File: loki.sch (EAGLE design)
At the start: 53 parts, among them IC2 LM358D, Q1 MOSFET-PCHANNELSMD, U1 USD SOCKET, X1 USBSMD, Y1 XRCGB_XTAL

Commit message: Minor layout changes; improvements to 2 pin plank template.
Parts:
- R3: device resistor:R-US_R0805 -> resistor:R-US_R0603
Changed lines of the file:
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@@
 <part name="GND18" library="supply1" deviceset="GND" device=""/>
 <part name="LED1" library="led" deviceset="LED" device="CHIP-LED0805"/>
-<part name="R3" library="resistor" deviceset="R-US_" device="R0805" value="330"/>
+<part name="R3" library="resistor" deviceset="R-US_" device="R0603" value="330"/>
 <part name="GND19" library="supply1" deviceset="GND" device=""/>
 <part name="SV1" library="con-lsta" deviceset="FE10-1" device=""/>

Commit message: Added reverse polarity protection diode.
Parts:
- added D3: (no value), adafruit:DIODESMA
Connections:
- new net N$11: CN1.PWR, D3.A
- net V+: now also D3.C; no longer CN1.PWR
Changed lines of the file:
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@@
 <part name="VCC1" library="supply1" deviceset="+3V3" device=""/>
 <part name="FRAME1" library="SparkFun-Aesthetics" deviceset="FRAME-A3" device=""/>
+<part name="D3" library="adafruit" deviceset="DIODE" device="SMA"/>
 </parts>
 <sheets>
@@
 <instance part="VCC1" gate="G$1" x="457.2" y="198.12"/>
 <instance part="FRAME1" gate="G$1" x="279.4" y="-45.72"/>
+<instance part="D3" gate="G$1" x="556.26" y="182.88"/>
 </instances>
 <busses>
@@
 <junction x="563.88" y="182.88"/>
 <junction x="561.34" y="182.88"/>
-<pinref part="CN1" gate="G$1" pin="PWR"/>
-<wire x1="561.34" y1="182.88" x2="551.18" y2="182.88" width="0.1524" layer="91"/>
+<pinref part="D3" gate="G$1" pin="C"/>
+<wire x1="558.8" y1="182.88" x2="561.34" y2="182.88" width="0.1524" layer="91"/>
 </segment>
 <segment>
@@
 </segment>
 </net>
+<net name="N$11" class="0">
+<segment>
+<pinref part="CN1" gate="G$1" pin="PWR"/>
+<pinref part="D3" gate="G$1" pin="A"/>
+<wire x1="551.18" y1="182.88" x2="553.72" y2="182.88" width="0.1524" layer="91"/>
+</segment>
+</net>

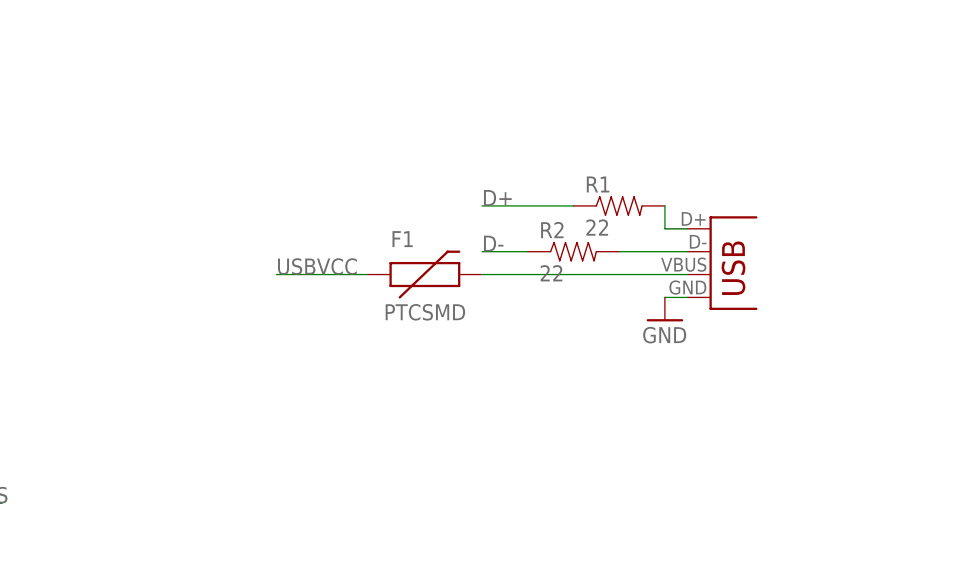
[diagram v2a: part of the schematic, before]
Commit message: Replace usb mini connector with usb micro one.
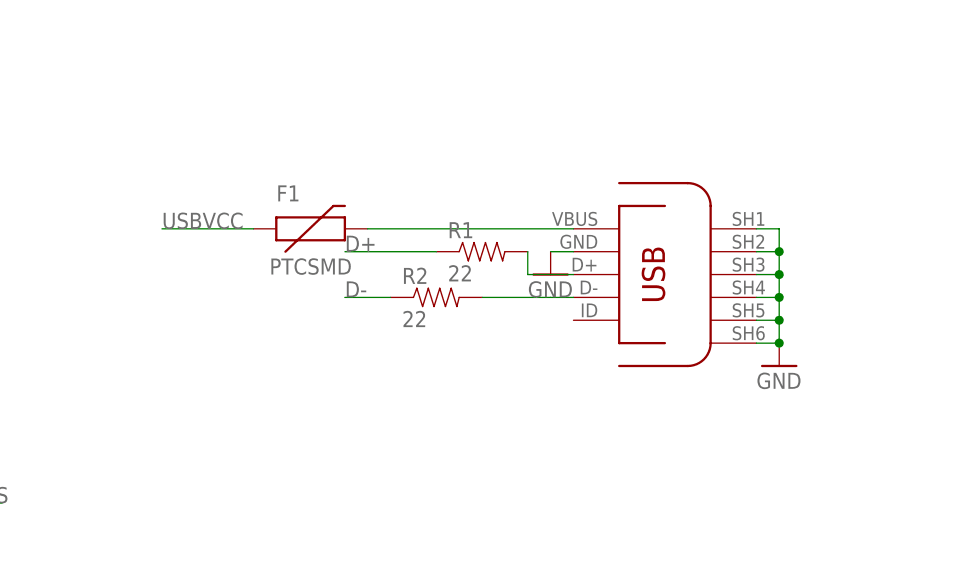
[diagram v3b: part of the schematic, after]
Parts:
- removed X1: USBSMD, SparkFun-Connectors:USBSMD
- added U$7: MICROUSB, ondraster:MICROUSB
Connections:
- net GND: now also U$7.GND, U$7.SH@1, U$7.SH@2, U$7.SH@3, U$7.SH@4, U$7.SH@5, U$7.SH@6; no longer X1.GND
- net N$15: now also U$7.VCC; no longer X1.VBUS
- net N$2: now also U$7.D-; no longer X1.D-
- net N$4: now also U$7.D+; no longer X1.D+
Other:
- moved on the sheet: F1, R1, R2
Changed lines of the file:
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@@
 <part name="R1" library="SparkFun-Passives" deviceset="RESISTOR" device="0603-RES" value="22"/>
 <part name="R2" library="SparkFun-Passives" deviceset="RESISTOR" device="0603-RES" value="22"/>
-<part name="X1" library="SparkFun-Connectors" deviceset="USB" device="SMD"/>
 <part name="P+1" library="supply1" deviceset="+3V3" device=""/>
 <part name="C3" library="resistor" deviceset="C-EU" device="C0603K" value="0.1u"/>
@@
 <part name="FRAME1" library="SparkFun-Aesthetics" deviceset="FRAME-A3" device=""/>
 <part name="D3" library="adafruit" deviceset="DIODE" device="SMA"/>
+<part name="U$7" library="ondraster" deviceset="MICROUSB" device=""/>
+<part name="GND2" library="supply1" deviceset="GND" device=""/>
 </parts>
 <sheets>
@@
 </plain>
 <instances>
-<instance part="R1" gate="G$1" x="482.6" y="101.6"/>
-<instance part="R2" gate="G$1" x="477.52" y="96.52"/>
-<instance part="X1" gate="G$1" x="492.76" y="91.44"/>
+<instance part="R1" gate="G$1" x="467.36" y="96.52"/>
+<instance part="R2" gate="G$1" x="462.28" y="91.44"/>
 <instance part="P+1" gate="G$1" x="309.88" y="71.12" rot="R90"/>
 <instance part="C3" gate="G$1" x="332.74" y="66.04"/>
@@
 <instance part="GND8" gate="1" x="464.82" y="180.34"/>
 <instance part="C17" gate="G$1" x="457.2" y="190.5"/>
-<instance part="GND9" gate="1" x="487.68" y="88.9"/>
+<instance part="GND9" gate="1" x="474.98" y="93.98"/>
 <instance part="U$3" gate="G$1" x="579.12" y="172.72"/>
 <instance part="P+5" gate="1" x="561.34" y="187.96"/>
@@
 <instance part="GND13" gate="1" x="614.68" y="22.86"/>
 <instance part="P+10" gate="1" x="647.7" y="58.42"/>
-<instance part="F1" gate="G$1" x="459.74" y="93.98"/>
+<instance part="F1" gate="G$1" x="447.04" y="99.06"/>
 <instance part="CN1" gate="G$1" x="548.64" y="180.34"/>
 <instance part="Y1" gate="G$1" x="388.62" y="104.14" rot="R90"/>
@@
 <instance part="FRAME1" gate="G$1" x="279.4" y="-45.72"/>
 <instance part="D3" gate="G$1" x="556.26" y="182.88"/>
+<instance part="U$7" gate="G$1" x="482.6" y="93.98" rot="MR0"/>
+<instance part="GND2" gate="1" x="500.38" y="83.82"/>
 </instances>
 <busses>
@@
 </segment>
 <segment>
-<pinref part="X1" gate="G$1" pin="GND"/>
 <pinref part="GND9" gate="1" pin="GND"/>
-<wire x1="490.22" y1="91.44" x2="487.68" y2="91.44" width="0.1524" layer="91"/>
+<wire x1="477.52" y1="96.52" x2="474.98" y2="96.52" width="0.1524" layer="91"/>
+<pinref part="U$7" gate="G$1" pin="GND"/>
 </segment>
 <segment>
@@
 <junction x="383.54" y="7.62"/>
 </segment>
+<segment>
+<pinref part="U$7" gate="G$1" pin="SH@1"/>
+<pinref part="GND2" gate="1" pin="GND"/>
+<wire x1="497.84" y1="99.06" x2="500.38" y2="99.06" width="0.1524" layer="91"/>
+<wire x1="500.38" y1="99.06" x2="500.38" y2="96.52" width="0.1524" layer="91"/>
+<pinref part="U$7" gate="G$1" pin="SH@6"/>
+<wire x1="500.38" y1="96.52" x2="500.38" y2="93.98" width="0.1524" layer="91"/>
+<wire x1="500.38" y1="93.98" x2="500.38" y2="91.44" width="0.1524" layer="91"/>
+<wire x1="500.38" y1="91.44" x2="500.38" y2="88.9" width="0.1524" layer="91"/>
+<wire x1="500.38" y1="88.9" x2="500.38" y2="86.36" width="0.1524" layer="91"/>
+<wire x1="500.38" y1="86.36" x2="497.84" y2="86.36" width="0.1524" layer="91"/>
+<junction x="500.38" y="86.36"/>
+<pinref part="U$7" gate="G$1" pin="SH@5"/>
+<wire x1="500.38" y1="88.9" x2="497.84" y2="88.9" width="0.1524" layer="91"/>
+<junction x="500.38" y="88.9"/>
+<pinref part="U$7" gate="G$1" pin="SH@4"/>
+<wire x1="500.38" y1="91.44" x2="497.84" y2="91.44" width="0.1524" layer="91"/>
+<junction x="500.38" y="91.44"/>
+<pinref part="U$7" gate="G$1" pin="SH@3"/>
+<wire x1="500.38" y1="93.98" x2="497.84" y2="93.98" width="0.1524" layer="91"/>
+<junction x="500.38" y="93.98"/>
+<pinref part="U$7" gate="G$1" pin="SH@2"/>
+<wire x1="500.38" y1="96.52" x2="497.84" y2="96.52" width="0.1524" layer="91"/>
+<junction x="500.38" y="96.52"/>
+</segment>
 </net>
 <net name="+5V" class="0">
@@
 <net name="N$2" class="0">
 <segment>
-<pinref part="X1" gate="G$1" pin="D-"/>
 <pinref part="R2" gate="G$1" pin="2"/>
-<wire x1="490.22" y1="96.52" x2="482.6" y2="96.52" width="0.1524" layer="91"/>
+<wire x1="474.98" y1="91.44" x2="467.36" y2="91.44" width="0.1524" layer="91"/>
+<pinref part="U$7" gate="G$1" pin="D-"/>
+<wire x1="477.52" y1="91.44" x2="474.98" y2="91.44" width="0.1524" layer="91"/>
 </segment>
 </net>
@@
 <segment>
 <pinref part="R1" gate="G$1" pin="2"/>
-<wire x1="487.68" y1="101.6" x2="487.68" y2="99.06" width="0.1524" layer="91"/>
-<pinref part="X1" gate="G$1" pin="D+"/>
-<wire x1="487.68" y1="99.06" x2="490.22" y2="99.06" width="0.1524" layer="91"/>
+<wire x1="472.44" y1="96.52" x2="472.44" y2="93.98" width="0.1524" layer="91"/>
+<wire x1="472.44" y1="93.98" x2="474.98" y2="93.98" width="0.1524" layer="91"/>
+<pinref part="U$7" gate="G$1" pin="D+"/>
+<wire x1="474.98" y1="93.98" x2="477.52" y2="93.98" width="0.1524" layer="91"/>
 </segment>
 </net>
@@
 <segment>
 <pinref part="R1" gate="G$1" pin="1"/>
-<wire x1="477.52" y1="101.6" x2="467.36" y2="101.6" width="0.1524" layer="91"/>
-<label x="467.36" y="101.6" size="1.778" layer="95"/>
+<wire x1="462.28" y1="96.52" x2="452.12" y2="96.52" width="0.1524" layer="91"/>
+<label x="452.12" y="96.52" size="1.778" layer="95"/>
 </segment>
 <segment>
@@
 <segment>
 <pinref part="R2" gate="G$1" pin="1"/>
-<wire x1="467.36" y1="96.52" x2="472.44" y2="96.52" width="0.1524" layer="91"/>
-<label x="467.36" y="96.52" size="1.778" layer="95"/>
+<wire x1="452.12" y1="91.44" x2="457.2" y2="91.44" width="0.1524" layer="91"/>
+<label x="452.12" y="91.44" size="1.778" layer="95"/>
 </segment>
 <segment>
@@
 <segment>
 <pinref part="F1" gate="G$1" pin="1"/>
-<wire x1="454.66" y1="93.98" x2="444.5" y2="93.98" width="0.1524" layer="91"/>
-<label x="444.5" y="93.98" size="1.778" layer="95"/>
+<wire x1="441.96" y1="99.06" x2="431.8" y2="99.06" width="0.1524" layer="91"/>
+<label x="431.8" y="99.06" size="1.778" layer="95"/>
 </segment>
 </net>
 <net name="N$15" class="0">
 <segment>
-<pinref part="X1" gate="G$1" pin="VBUS"/>
 <pinref part="F1" gate="G$1" pin="2"/>
-<wire x1="490.22" y1="93.98" x2="467.36" y2="93.98" width="0.1524" layer="91"/>
-</segment>
-</net>
+<wire x1="477.52" y1="99.06" x2="454.66" y2="99.06" width="0.1524" layer="91"/>
+<pinref part="U$7" gate="G$1" pin="VCC"/>
+</segment>
+</net>

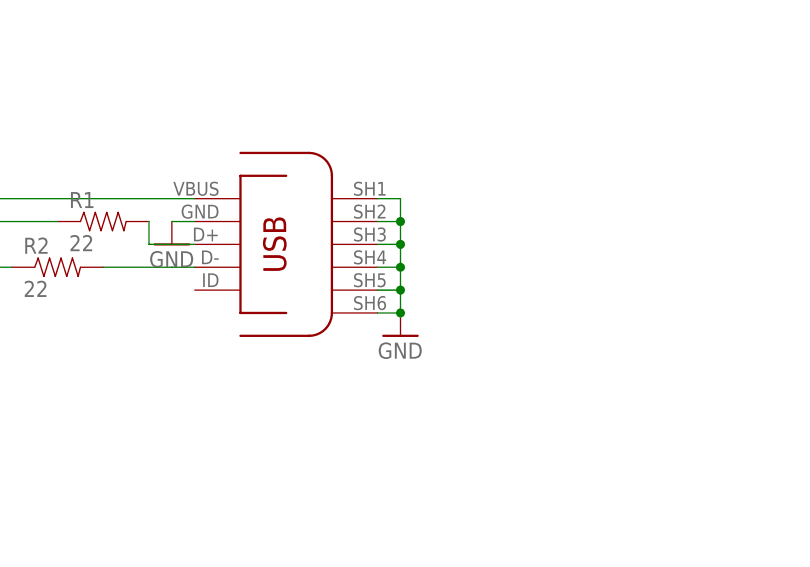
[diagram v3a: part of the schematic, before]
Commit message: Widened a few traces where possible.
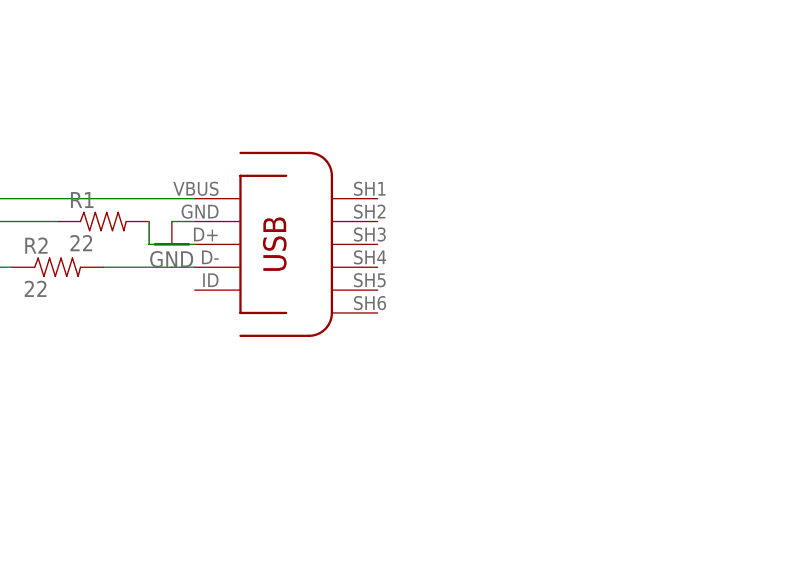
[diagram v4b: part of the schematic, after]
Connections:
- net GND: no longer U$7.SH@1, U$7.SH@2, U$7.SH@3, U$7.SH@4, U$7.SH@5, U$7.SH@6
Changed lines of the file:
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@@
 <part name="D3" library="adafruit" deviceset="DIODE" device="SMA"/>
 <part name="U$7" library="ondraster" deviceset="MICROUSB" device=""/>
-<part name="GND2" library="supply1" deviceset="GND" device=""/>
 </parts>
 <sheets>
@@
 <instance part="D3" gate="G$1" x="556.26" y="182.88"/>
 <instance part="U$7" gate="G$1" x="482.6" y="93.98" rot="MR0"/>
-<instance part="GND2" gate="1" x="500.38" y="83.82"/>
 </instances>
 <busses>
@@
 <junction x="383.54" y="7.62"/>
 </segment>
-<segment>
-<pinref part="U$7" gate="G$1" pin="SH@1"/>
-<pinref part="GND2" gate="1" pin="GND"/>
-<wire x1="497.84" y1="99.06" x2="500.38" y2="99.06" width="0.1524" layer="91"/>
-<wire x1="500.38" y1="99.06" x2="500.38" y2="96.52" width="0.1524" layer="91"/>
-<pinref part="U$7" gate="G$1" pin="SH@6"/>
-<wire x1="500.38" y1="96.52" x2="500.38" y2="93.98" width="0.1524" layer="91"/>
-<wire x1="500.38" y1="93.98" x2="500.38" y2="91.44" width="0.1524" layer="91"/>
-<wire x1="500.38" y1="91.44" x2="500.38" y2="88.9" width="0.1524" layer="91"/>
-<wire x1="500.38" y1="88.9" x2="500.38" y2="86.36" width="0.1524" layer="91"/>
-<wire x1="500.38" y1="86.36" x2="497.84" y2="86.36" width="0.1524" layer="91"/>
-<junction x="500.38" y="86.36"/>
-<pinref part="U$7" gate="G$1" pin="SH@5"/>
-<wire x1="500.38" y1="88.9" x2="497.84" y2="88.9" width="0.1524" layer="91"/>
-<junction x="500.38" y="88.9"/>
-<pinref part="U$7" gate="G$1" pin="SH@4"/>
-<wire x1="500.38" y1="91.44" x2="497.84" y2="91.44" width="0.1524" layer="91"/>
-<junction x="500.38" y="91.44"/>
-<pinref part="U$7" gate="G$1" pin="SH@3"/>
-<wire x1="500.38" y1="93.98" x2="497.84" y2="93.98" width="0.1524" layer="91"/>
-<junction x="500.38" y="93.98"/>
-<pinref part="U$7" gate="G$1" pin="SH@2"/>
-<wire x1="500.38" y1="96.52" x2="497.84" y2="96.52" width="0.1524" layer="91"/>
-<junction x="500.38" y="96.52"/>
-</segment>
 </net>
